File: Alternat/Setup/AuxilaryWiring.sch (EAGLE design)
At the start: 7 parts

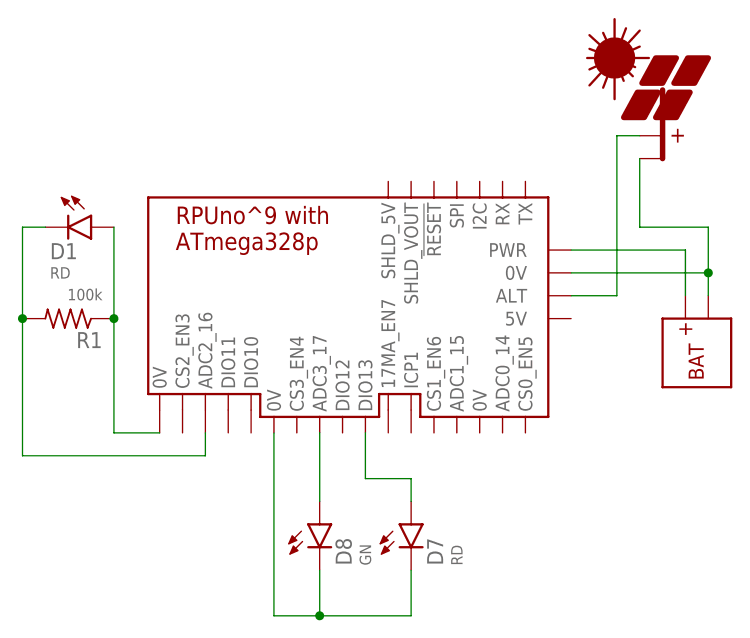
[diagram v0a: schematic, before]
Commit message: Solenoid: voltage divider on SLP003 solar pannel for light sensor
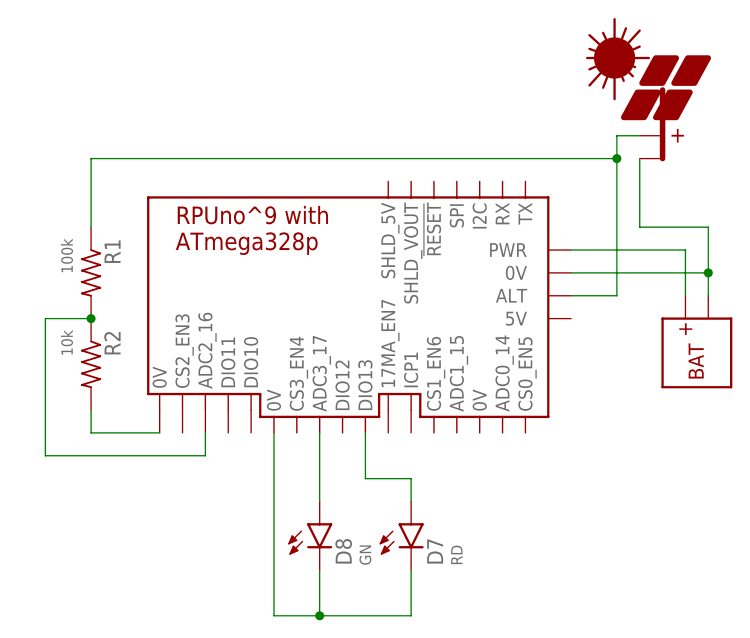
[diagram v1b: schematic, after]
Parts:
- removed D1: RD, D-LED:LED5MM
- added R2: 10k, R-C:R0805
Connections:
- net N$1: now also R2.2; no longer D1.A, R1.1
- net N$2: now also R2.1; no longer D1.K
- net N$50: now also R1.1
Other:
- note added: "LIGHT SENSOR"
- note removed: "SENSOR"
- moved on the sheet: R1
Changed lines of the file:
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@@
 <part name="U$7" library="Documentation" deviceset="BAT" device=""/>
 <part name="BM1" library="Documentation" deviceset="RPUNO" device=""/>
-<part name="D1" library="D-LED" deviceset="LED" device="5MM" value="RD"/>
+<part name="R2" library="R-C" deviceset="R" device="0805" value="10k"/>
 </parts>
 <sheets>
@@
 <text x="57.404" y="78.232" size="1.778" layer="98" rot="R90">STATUS</text>
 <text x="32.004" y="70.612" size="1.778" layer="98" rot="R90">DAYNIGHT_STATUS</text>
-<text x="6.35" y="121.92" size="1.778" layer="98">SENSOR</text>
+<text x="13.97" y="88.9" size="1.778" layer="98" rot="R180">LIGHT
+SENSOR</text>
 </plain>
 <instances>
-<instance part="R1" gate="G$1" x="10.16" y="106.68" rot="R180"/>
+<instance part="R1" gate="G$1" x="12.7" y="111.76" rot="R270"/>
 <instance part="D8" gate="G$1" x="38.1" y="83.82"/>
 <instance part="D7" gate="G$1" x="48.26" y="83.82"/>
@@
 <instance part="U$7" gate="G$1" x="81.28" y="101.6" rot="R90"/>
 <instance part="BM1" gate="G$1" x="45.72" y="109.22"/>
-<instance part="D1" gate="G$1" x="12.7" y="116.84" rot="R270"/>
+<instance part="R2" gate="G$1" x="12.7" y="101.6" rot="R270"/>
 </instances>
 <busses>
@@
 <segment>
 <pinref part="PV4" gate="G$1" pin="+PV"/>
-<wire x1="71.12" y1="109.22" x2="71.12" y2="127" width="0.1524" layer="91"/>
+<wire x1="71.12" y1="109.22" x2="71.12" y2="124.46" width="0.1524" layer="91"/>
+<wire x1="71.12" y1="124.46" x2="71.12" y2="127" width="0.1524" layer="91"/>
 <wire x1="71.12" y1="127" x2="73.66" y2="127" width="0.1524" layer="91"/>
 <wire x1="71.12" y1="109.22" x2="66.04" y2="109.22" width="0.1524" layer="91"/>
 <pinref part="BM1" gate="G$1" pin="ALT"/>
+<pinref part="R1" gate="G$1" pin="1"/>
+<wire x1="12.7" y1="116.84" x2="12.7" y2="124.46" width="0.1524" layer="91"/>
+<wire x1="12.7" y1="124.46" x2="71.12" y2="124.46" width="0.1524" layer="91"/>
+<junction x="71.12" y="124.46"/>
 </segment>
 </net>
@@
 <segment>
 <pinref part="BM1" gate="G$1" pin="0V@5"/>
-<wire x1="20.32" y1="93.98" x2="15.24" y2="93.98" width="0.1524" layer="91"/>
-<pinref part="R1" gate="G$1" pin="1"/>
-<wire x1="15.24" y1="93.98" x2="15.24" y2="106.68" width="0.1524" layer="91"/>
-<pinref part="D1" gate="G$1" pin="A"/>
-<wire x1="15.24" y1="106.68" x2="15.24" y2="116.84" width="0.1524" layer="91"/>
-<junction x="15.24" y="106.68"/>
+<wire x1="20.32" y1="93.98" x2="12.7" y2="93.98" width="0.1524" layer="91"/>
+<pinref part="R2" gate="G$1" pin="2"/>
+<wire x1="12.7" y1="93.98" x2="12.7" y2="96.52" width="0.1524" layer="91"/>
 </segment>
 </net>
 <net name="N$2" class="0">
 <segment>
-<pinref part="D1" gate="G$1" pin="K"/>
 <pinref part="R1" gate="G$1" pin="2"/>
-<wire x1="7.62" y1="116.84" x2="5.08" y2="116.84" width="0.1524" layer="91"/>
-<wire x1="5.08" y1="116.84" x2="5.08" y2="106.68" width="0.1524" layer="91"/>
-<wire x1="5.08" y1="106.68" x2="5.08" y2="91.44" width="0.1524" layer="91"/>
-<junction x="5.08" y="106.68"/>
+<wire x1="12.7" y1="106.68" x2="7.62" y2="106.68" width="0.1524" layer="91"/>
+<wire x1="7.62" y1="106.68" x2="7.62" y2="91.44" width="0.1524" layer="91"/>
 <pinref part="BM1" gate="G$1" pin="ADC2_16"/>
-<wire x1="5.08" y1="91.44" x2="25.4" y2="91.44" width="0.1524" layer="91"/>
+<wire x1="7.62" y1="91.44" x2="25.4" y2="91.44" width="0.1524" layer="91"/>
 <wire x1="25.4" y1="91.44" x2="25.4" y2="93.98" width="0.1524" layer="91"/>
+<pinref part="R2" gate="G$1" pin="1"/>
+<junction x="12.7" y="106.68"/>
 </segment>
 </net>
